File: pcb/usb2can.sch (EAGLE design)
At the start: 48 parts, among them CON1 USB_A_MALESMD, IC1 ADM3053M, IC2 LD1117S33

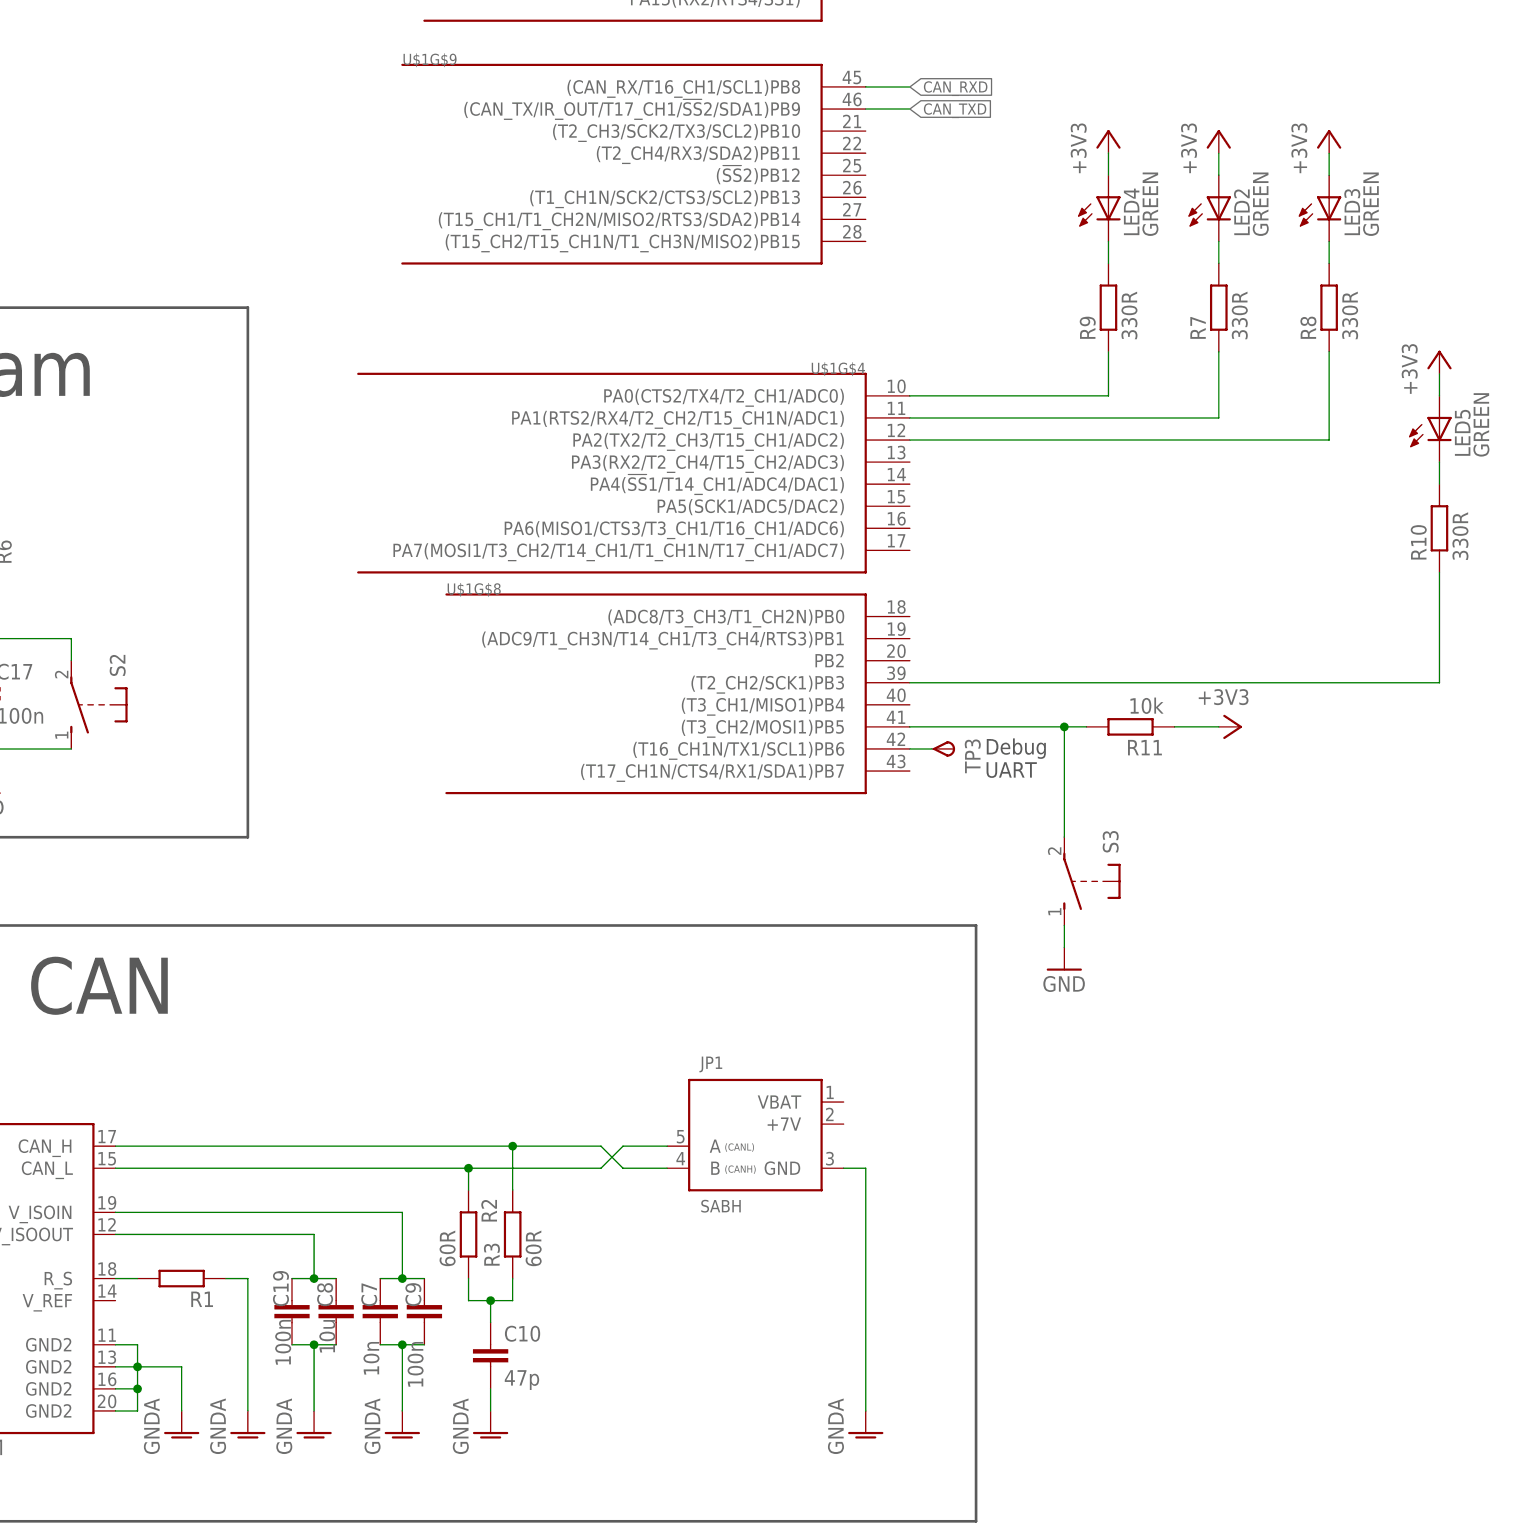
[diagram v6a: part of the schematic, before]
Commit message: pcb: update schematic with correct values
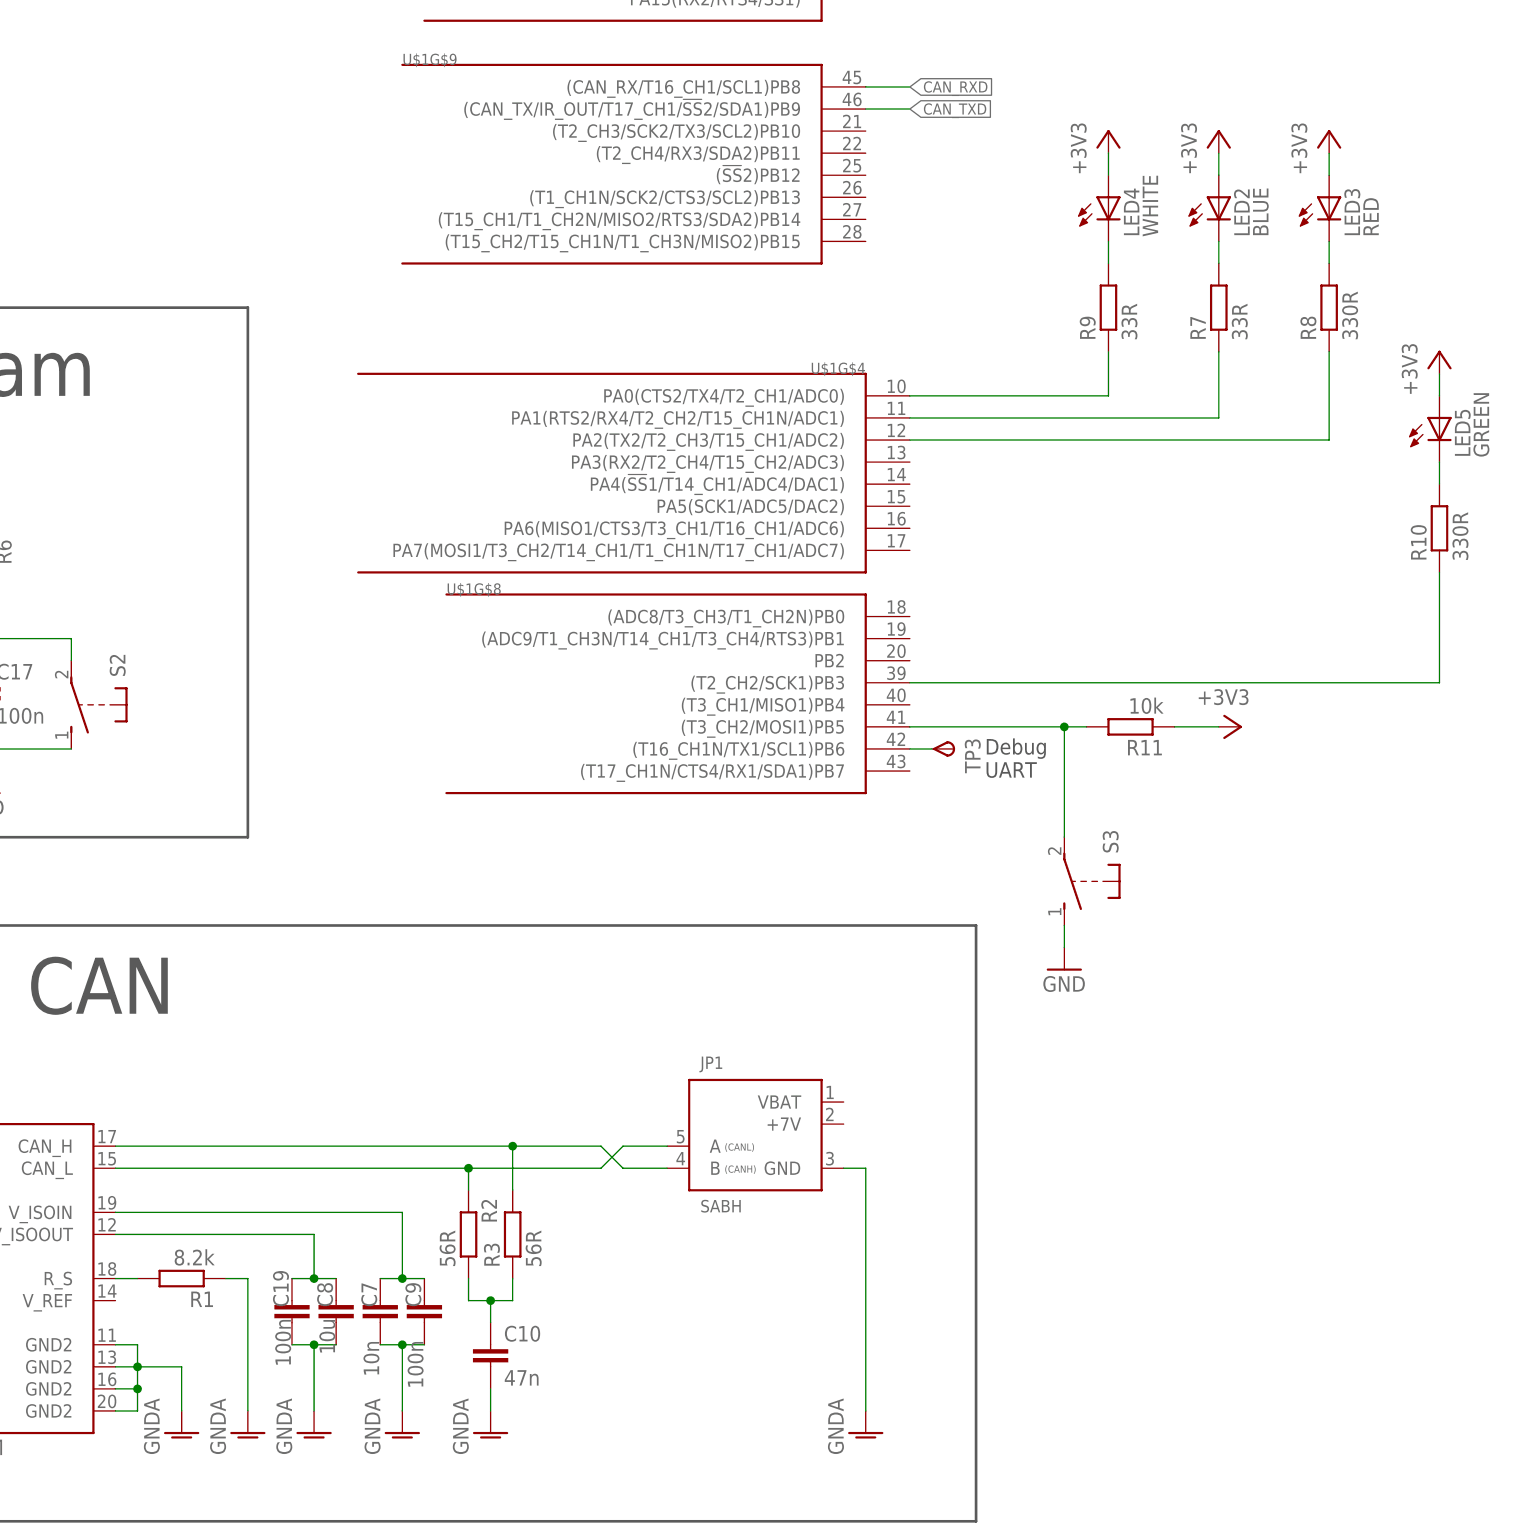
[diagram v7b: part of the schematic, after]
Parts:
- C10: value 47p -> 47n
- LED2: value GREEN -> BLUE
- LED3: value GREEN -> RED
- LED4: value GREEN -> WHITE
- R1: value (none) -> 8.2k
- R2, R3: value 60R -> 56R
- R7, R9: value 330R -> 33R
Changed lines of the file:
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@@
 <part name="+3V2" library="supply1" deviceset="+3V3" device=""/>
 <part name="GND6" library="supply1" deviceset="GNDA" device=""/>
-<part name="R1" library="rcl" deviceset="R-EU_" device="R0603"/>
+<part name="R1" library="rcl" deviceset="R-EU_" device="R0603" value="8.2k"/>
 <part name="GND7" library="supply1" deviceset="GNDA" device=""/>
 <part name="GND8" library="supply1" deviceset="GNDA" device=""/>
@@
 <part name="U$1" library="stm32" deviceset="STM32F072C" device="T"/>
 <part name="GND9" library="supply1" deviceset="GNDA" device=""/>
-<part name="R2" library="rcl" deviceset="R-EU_" device="R0805" value="60R"/>
-<part name="R3" library="rcl" deviceset="R-EU_" device="R0805" value="60R"/>
-<part name="C10" library="rcl" deviceset="C-EU" device="C0603K" value="47p"/>
+<part name="R2" library="rcl" deviceset="R-EU_" device="R0805" value="56R"/>
+<part name="R3" library="rcl" deviceset="R-EU_" device="R0805" value="56R"/>
+<part name="C10" library="rcl" deviceset="C-EU" device="C0603K" value="47n"/>
 <part name="GND10" library="supply1" deviceset="GNDA" device=""/>
 <part name="C11" library="rcl" deviceset="C-EU" device="C0603" value="100n"/>
@@
 <part name="C19" library="rcl" deviceset="C-EU" device="C0805K" value="100n"/>
 <part name="GND19" library="supply1" deviceset="GNDA" device=""/>
-<part name="LED2" library="led" deviceset="LED" device="CHIPLED_0603" value="GREEN"/>
+<part name="LED2" library="led" deviceset="LED" device="CHIPLED_0603" value="BLUE"/>
 <part name="+3V9" library="supply1" deviceset="+3V3" device=""/>
-<part name="R7" library="resistor" deviceset="R-EU_" device="R0603" value="330R"/>
+<part name="R7" library="resistor" deviceset="R-EU_" device="R0603" value="33R"/>
 <part name="S3" library="micro_switch" deviceset="MICRO_SWITCH_3X6X2.5" device="S"/>
 <part name="GND20" library="supply1" deviceset="GND" device=""/>
-<part name="LED3" library="led" deviceset="LED" device="CHIPLED_0603" value="GREEN"/>
+<part name="LED3" library="led" deviceset="LED" device="CHIPLED_0603" value="RED"/>
 <part name="+3V10" library="supply1" deviceset="+3V3" device=""/>
 <part name="R8" library="resistor" deviceset="R-EU_" device="R0603" value="330R"/>
-<part name="LED4" library="led" deviceset="LED" device="CHIPLED_0603" value="GREEN"/>
+<part name="LED4" library="led" deviceset="LED" device="CHIPLED_0603" value="WHITE"/>
 <part name="+3V11" library="supply1" deviceset="+3V3" device=""/>
-<part name="R9" library="resistor" deviceset="R-EU_" device="R0603" value="330R"/>
+<part name="R9" library="resistor" deviceset="R-EU_" device="R0603" value="33R"/>
 <part name="LED5" library="led" deviceset="LED" device="CHIPLED_0603" value="GREEN"/>
 <part name="+3V12" library="supply1" deviceset="+3V3" device=""/>

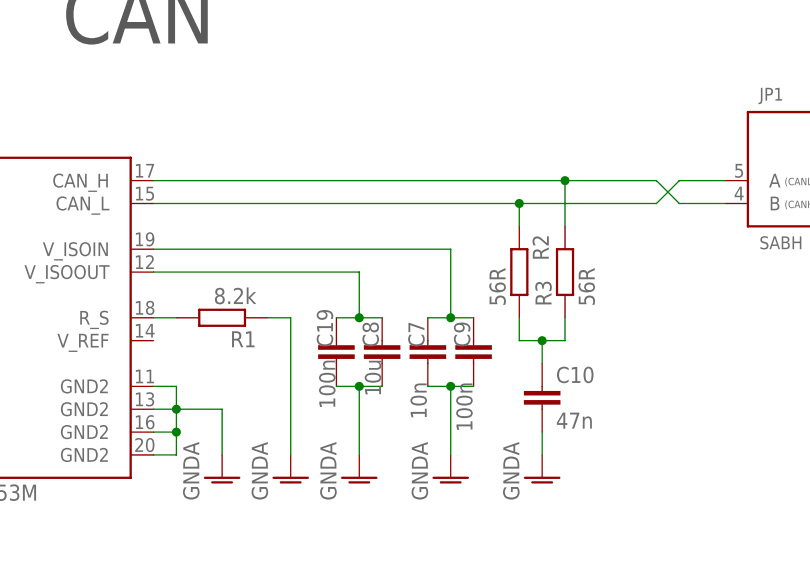
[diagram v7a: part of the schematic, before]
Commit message: pcb: fix CAN transceiver V_ISOIN and V_ISOOUT not connected
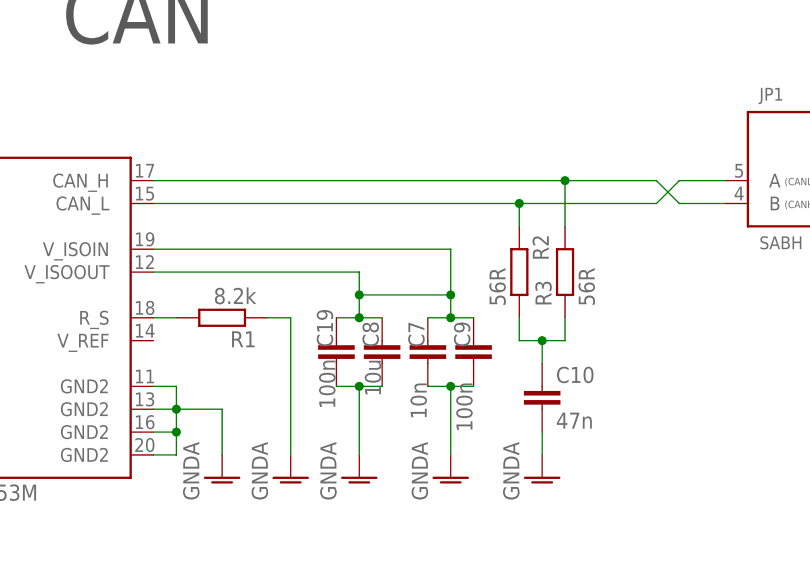
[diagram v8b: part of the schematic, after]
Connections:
- removed net N$10: C7.1, C9.1, IC1.V_ISOIN
- net N$8: now also C7.1, C9.1, IC1.V_ISOIN
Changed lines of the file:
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@@
 <wire x1="139.7" y1="7.62" x2="142.24" y2="7.62" width="0.1524" layer="91"/>
 <wire x1="142.24" y1="7.62" x2="144.78" y2="7.62" width="0.1524" layer="91"/>
-<wire x1="142.24" y1="7.62" x2="142.24" y2="12.7" width="0.1524" layer="91"/>
+<wire x1="142.24" y1="7.62" x2="142.24" y2="10.16" width="0.1524" layer="91"/>
 <junction x="142.24" y="7.62"/>
 <pinref part="IC1" gate="G$1" pin="V_ISOOUT"/>
+<wire x1="142.24" y1="10.16" x2="142.24" y2="12.7" width="0.1524" layer="91"/>
 <wire x1="142.24" y1="12.7" x2="119.38" y2="12.7" width="0.1524" layer="91"/>
-</segment>
-</net>
-<net name="N$10" class="0">
-<segment>
 <pinref part="C7" gate="G$1" pin="1"/>
 <pinref part="C9" gate="G$1" pin="1"/>
 <wire x1="149.86" y1="7.62" x2="152.4" y2="7.62" width="0.1524" layer="91"/>
 <wire x1="152.4" y1="7.62" x2="154.94" y2="7.62" width="0.1524" layer="91"/>
-<wire x1="152.4" y1="7.62" x2="152.4" y2="15.24" width="0.1524" layer="91"/>
+<wire x1="152.4" y1="7.62" x2="152.4" y2="10.16" width="0.1524" layer="91"/>
 <junction x="152.4" y="7.62"/>
 <pinref part="IC1" gate="G$1" pin="V_ISOIN"/>
+<wire x1="152.4" y1="10.16" x2="152.4" y2="15.24" width="0.1524" layer="91"/>
 <wire x1="152.4" y1="15.24" x2="119.38" y2="15.24" width="0.1524" layer="91"/>
+<wire x1="142.24" y1="10.16" x2="152.4" y2="10.16" width="0.1524" layer="91"/>
+<junction x="142.24" y="10.16"/>
+<junction x="152.4" y="10.16"/>
 </segment>
 </net>
